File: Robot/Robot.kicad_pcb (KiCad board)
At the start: 2 copper layers, 130 x 156 mm, 172 parts, among them J1 Servo1, J10 Lidar, J11 Console, J12 M1, J13 M2, J14 M3, J15 M4, J16 Battery, J17 DE9_Receptacle, J18 Balance, J2 Servo2, J3 Servo3, J4 Servo4, J5 Servo5, J6 Servo6, J7 Servo7, J8 Beacon, J9 DLED, Q1 DMP3036SSD, Q2 Si2003, SW1 User, SW2 Pwr, U1 ADC128D818, U10 SY8366HQQC, U11 SY8366HQQC, U12 SY8366HQQC, U13 INA180A2, U14 INA180A2, U15 INA180A2, U16 INA180A2, U2 MaixCAM2, U3 DRV8845RHHR, U4 ICE40UP5K-SG48ITR, U5 74HCT245, U6 MCP4728, U7 NC7SZ175, U8 TLV70212DBVR, U9 TMI6050-33

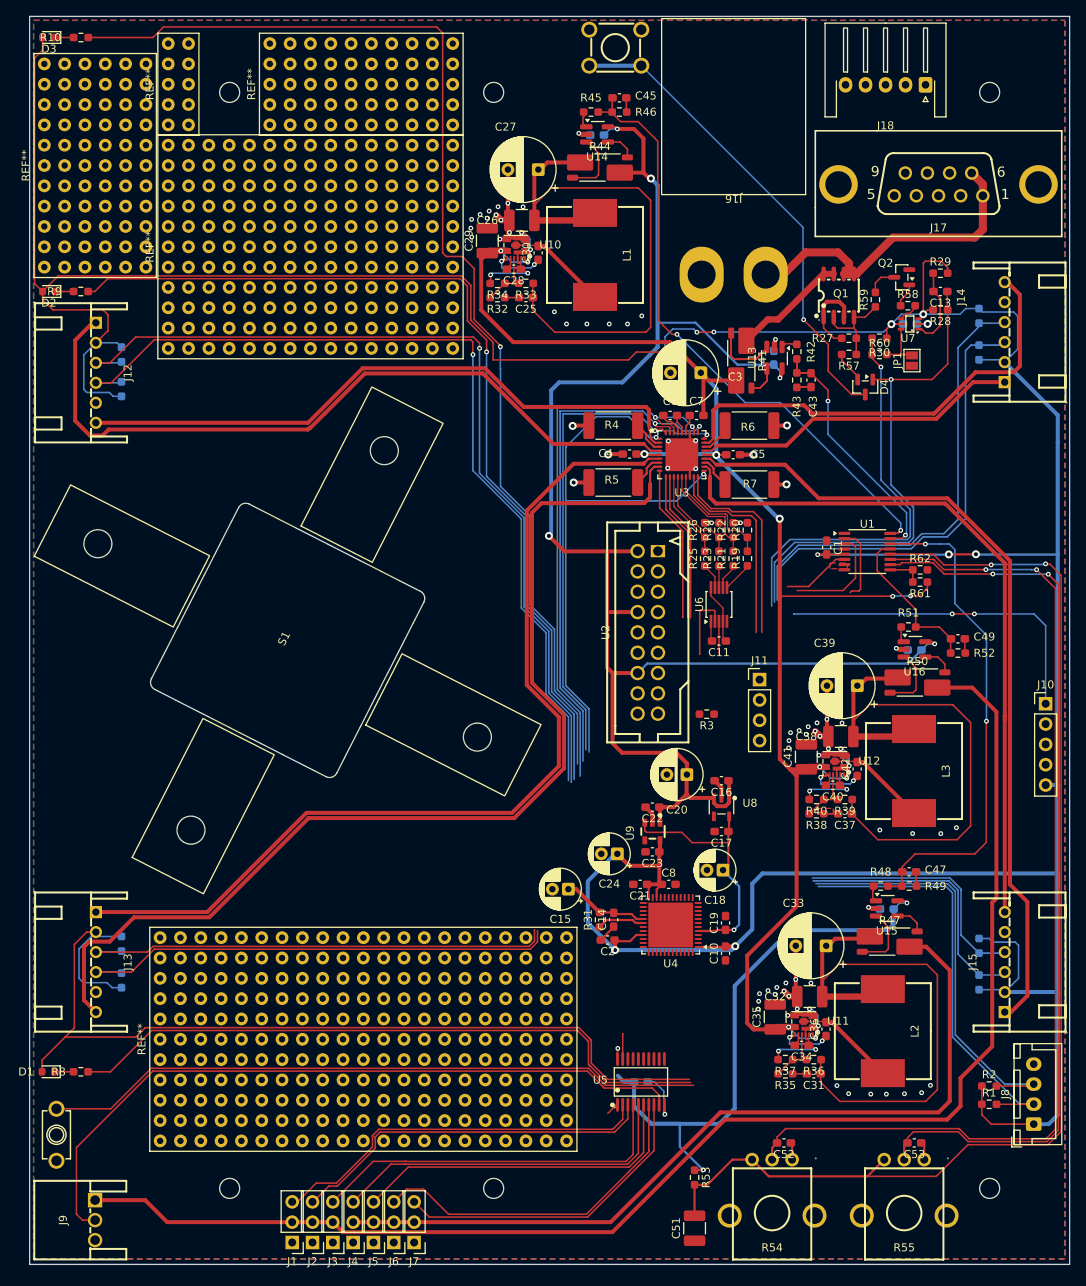
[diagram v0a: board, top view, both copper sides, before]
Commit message: Updated PCB for Robot (routing close to finish)
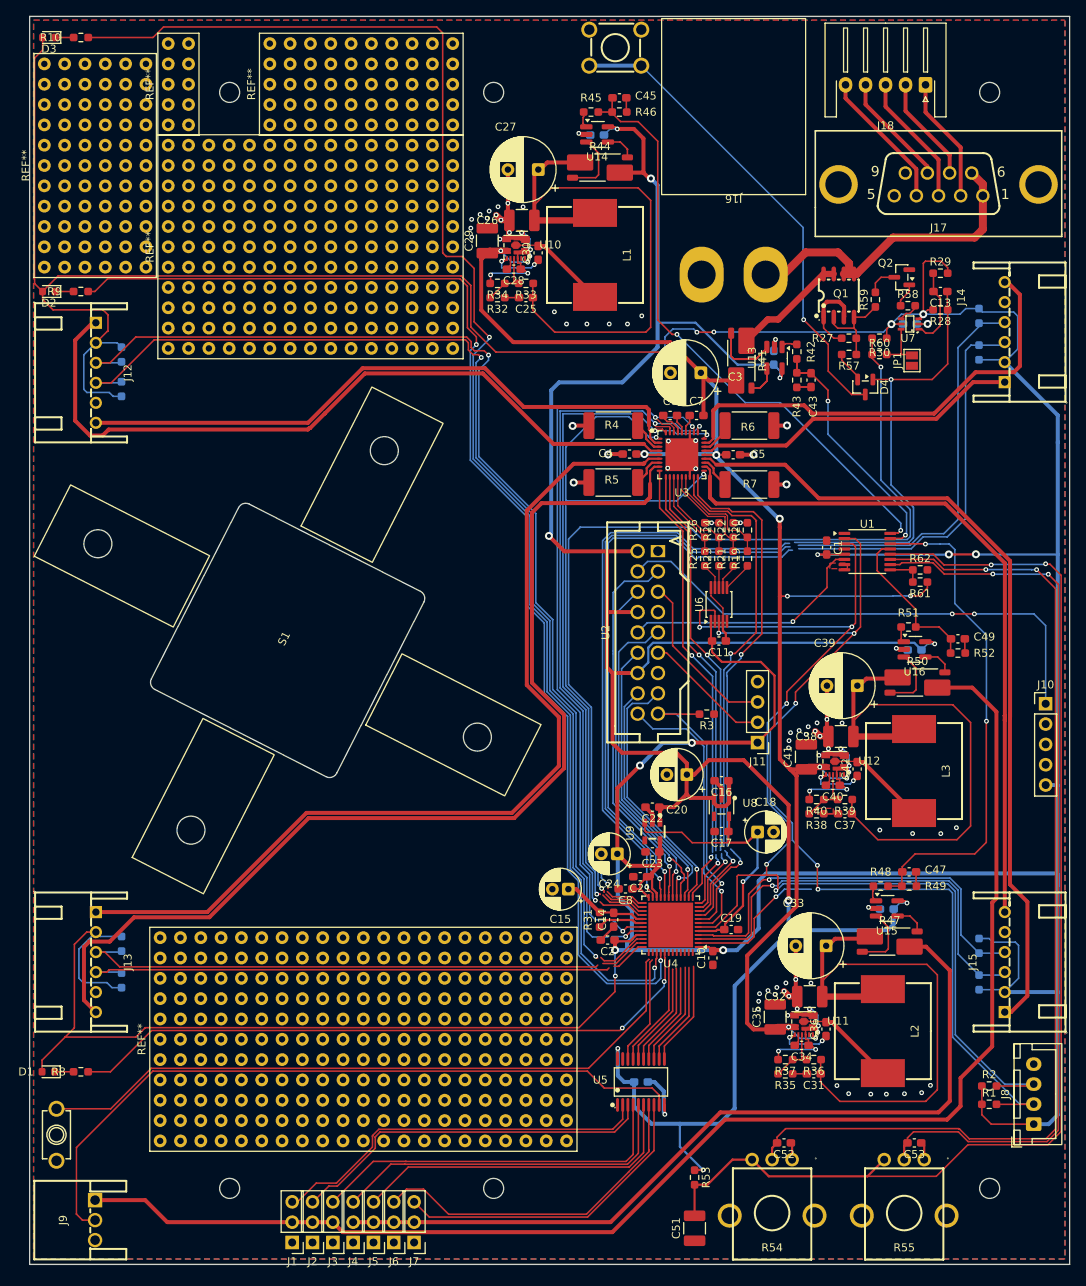
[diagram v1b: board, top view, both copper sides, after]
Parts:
- moved J11 7.88 mm to (126.0, 112.8), turned to 180 degrees
- moved C18 6.43 mm to (126.0, 124.0), turned to 0 degrees
- moved C8 5.43 mm to (109.5, 131.1), turned to 180 degrees
- moved C10 1.69 mm to (120.4, 139.7)
- moved C19 1.08 mm to (122.7, 136.1), turned to 0 degrees
- moved C21 0.95 mm to (111.3, 129.5)
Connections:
- R10 pad 2: Net-(U4A-RGB2) -> Net-(U4A-RGB0)
- R8 pad 2: Net-(U4A-RGB0) -> Net-(U4A-RGB2)
- U2 pad 3: /FPGA/CTRL_SYN -> /FPGA/CTRL_INT
- U2 pad 9: /FPGA/CTRL_INT -> /FPGA/CTRL_SYN
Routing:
- net Net-(U4A-RGB0): track 81.8 -> 184.3 mm, vias 0 -> 2
- net Net-(U3-PHASE1): track 25.6 -> 126.3 mm, vias 0 -> 2
- net Net-(U4B-IOB_23b): track 0.00 -> 85.0 mm, vias 0 -> 1
- net /FPGA/PWR_OFF: track 51.2 -> 126.9 mm, vias 1 -> 3
- net Net-(U4B-IOB_25b_G3): track 82.6 -> 157.4 mm, vias 0 -> 1
- net /FPGA/SCL: track 74.9 -> 148.8 mm, vias 0 -> 5
- net /FPGA/SDA: track 66.9 -> 136.7 mm, vias 0 -> 6
- net Net-(U4A-RGB2): track 144.7 -> 80.8 mm, vias 1 -> 2
- net /FPGA/CTRL_INT: track 0.00 -> 47.8 mm, vias 0 -> 1
- net /FPGA/DL_CS: track 0.00 -> 43.3 mm, vias 0 -> 1
- net /FPGA/CTRL_SYN: track 0.00 -> 39.8 mm, vias 0 -> 1
- net +3V3: track 620.5 -> 658.7 mm, vias 10 -> 13
- net Net-(U4A-RGB1): track 115.6 -> 153.8 mm, vias 1 -> 2
- net /FPGA/DL_CRESET: track 0.00 -> 37.5 mm, vias 0 -> 1
- net Net-(U3-PHASE4): track 19.6 -> 57.0 mm, vias 0 -> 1
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
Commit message: Updated PCB for Robot (routing finished, postprocessing in progress)
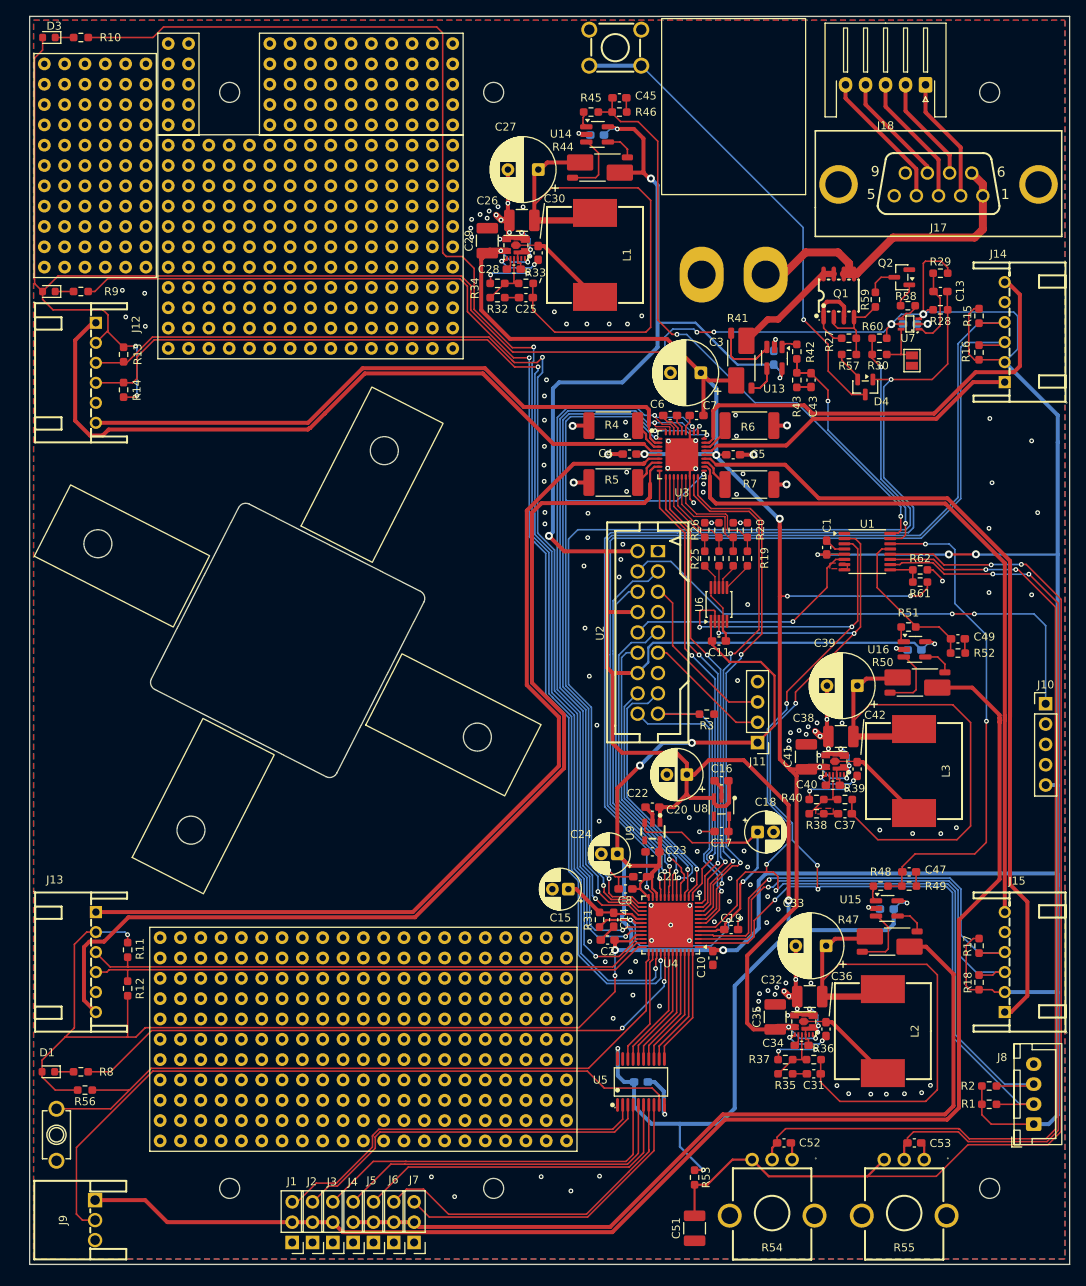
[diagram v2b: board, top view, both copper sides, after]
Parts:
- added R56: 1K, Resistor_SMD:R_0603_1608Metric_Pad0.98x0.95mm_HandSolder, F.Cu at (41.9, 156.2)
- J12, J13, J14, J15: footprint easyeda2kicad:CONN-TH_S6B-XH-A-1-LF-SN -> locals:CONN-TH_S6B-XH-A-1-LF-SN
- R11, R12, R13, R14, R15, R16, R17, R18: moved to F.Cu
- R54, R55: footprint easyeda2kicad:RES-TH_RK09K1130A6S -> locals:RES-TH_RK09K1130A6S
- moved R12 1.27 mm to (47.2, 143.5)
- moved R11 1.08 mm to (47.2, 138.7)
- moved R14 0.28 mm to (46.7, 68.7)
- moved R13 0.26 mm to (46.7, 64.3)
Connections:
- net Net-(J15A-C1) renamed /FPGA/FPGACore/P4
- net Net-(J15A-C2) renamed /FPGA/FPGACore/P3
- net Net-(U4A-IOT_49a) renamed /FPGA/FPGACore/P43
- J12 pad 3: Net-(J12A-C2) -> /FPGA/FPGACore/P32
- J12 pad 4: Net-(J12A-C1) -> /FPGA/FPGACore/P34
- J13 pad 3: Net-(J13A-C2) -> /FPGA/FPGACore/P35
- J13 pad 4: Net-(J13A-C1) -> /FPGA/FPGACore/P36
- J14 pad 3: Net-(J14A-C2) -> /FPGA/FPGACore/P20
- J14 pad 4: Net-(J14A-C1) -> /FPGA/FPGACore/P21
- R11 pad 1: Net-(J13A-C2) -> /FPGA/FPGACore/P35
- R12 pad 1: Net-(J13A-C1) -> /FPGA/FPGACore/P36
- R13 pad 1: Net-(J12A-C2) -> /FPGA/FPGACore/P32
- R14 pad 1: Net-(J12A-C1) -> /FPGA/FPGACore/P34
- R15 pad 1: Net-(J14A-C1) -> /FPGA/FPGACore/P21
- R16 pad 1: Net-(J14A-C2) -> /FPGA/FPGACore/P20
- SW1 pad 2: Net-(U4B-IOB_25b_G3) -> /FPGA/FPGACore/P37
- U3 pad 1: Net-(U3-I04) -> /FPGA/FPGACore/P26
- U3 pad 10: Net-(U3-PHASE3) -> /FPGA/FPGACore/P12
- U3 pad 11: Net-(U3-~{SLEEP}) -> /FPGA/FPGACore/P11
- U3 pad 17: Net-(U3-PHASE2) -> /FPGA/FPGACore/P10
- U3 pad 18: Net-(U3-PHASE1) -> /FPGA/FPGACore/P9
- U3 pad 19: Net-(U3-I04) -> /FPGA/FPGACore/P26
- U3 pad 27: Net-(U3-I03) -> /FPGA/FPGACore/P27
- U3 pad 28: Net-(U3-I02) -> /FPGA/FPGACore/P28
- U3 pad 29: Net-(U3-I01) -> /FPGA/FPGACore/P31
- U3 pad 34: Net-(U3-I01) -> /FPGA/FPGACore/P31
- U3 pad 35: Net-(U3-I02) -> /FPGA/FPGACore/P28
- U3 pad 36: Net-(U3-I03) -> /FPGA/FPGACore/P27
- U3 pad 9: Net-(U3-PHASE4) -> /FPGA/FPGACore/P13
- U4 pad 10: /FPGA/PWR_OFF -> /FPGA/FPGACore/P10
- U4 pad 11: Net-(U4B-IOB_20a) -> /FPGA/FPGACore/P11
- U4 pad 12: Net-(U4B-IOB_22a) -> /FPGA/FPGACore/P12
- U4 pad 13: /FPGA/PwrBtnInput -> /FPGA/FPGACore/P13
- U4 pad 2: Net-(J14A-C2) -> /FPGA/SDA
- U4 pad 20: Net-(U4B-IOB_25b_G3) -> /FPGA/FPGACore/P20
- U4 pad 21: Net-(U4B-IOB_23b) -> /FPGA/FPGACore/P21
- U4 pad 23: Net-(U3-PHASE1) -> /FPGA/PwrBtnInput
- U4 pad 25: Net-(U3-I01) -> /FPGA/PWR_OFF
- U4 pad 26: Net-(U3-PHASE2) -> /FPGA/FPGACore/P26
- U4 pad 27: Net-(U3-I02) -> /FPGA/FPGACore/P27
- U4 pad 28: Net-(U3-I03) -> /FPGA/FPGACore/P28
- U4 pad 31: Net-(U3-PHASE3) -> /FPGA/FPGACore/P31
- U4 pad 32: Net-(U3-I04) -> /FPGA/FPGACore/P32
- U4 pad 34: Net-(U3-PHASE4) -> /FPGA/FPGACore/P34
- U4 pad 35: Net-(U4A-IOT_46b_G0) -> /FPGA/FPGACore/P35
- U4 pad 36: Net-(U4A-IOT_48b) -> /FPGA/FPGACore/P36
- U4 pad 37: Net-(U3-~{SLEEP}) -> /FPGA/FPGACore/P37
- U4 pad 38: Net-(U4A-IOT_50b) -> /FPGA/FPGACore/P38
- U4 pad 42: Net-(U4A-IOT_51a) -> /FPGA/FPGACore/P42
- U4 pad 44: Net-(J13A-C1) -> /FPGA/FPGACore/P44
- U4 pad 45: Net-(J14A-C1) -> /FPGA/FPGACore/P45
- U4 pad 46: Net-(J12A-C1) -> /FPGA/FPGACore/P46
- U4 pad 47: Net-(J12A-C2) -> /FPGA/FPGACore/P47
- U4 pad 48: Net-(J13A-C2) -> /FPGA/FPGACore/P48
- U4 pad 9: /FPGA/SDA -> /FPGA/FPGACore/P9
- U5 pad 11: Net-(U4B-IOB_23b) -> /FPGA/FPGACore/P48
- U5 pad 12: Net-(U4B-IOB_22a) -> /FPGA/FPGACore/P47
- U5 pad 13: Net-(U4B-IOB_20a) -> /FPGA/FPGACore/P46
- U5 pad 14: Net-(U4A-IOT_51a) -> /FPGA/FPGACore/P45
- U5 pad 15: Net-(U4A-IOT_50b) -> /FPGA/FPGACore/P44
- U5 pad 17: Net-(U4A-IOT_48b) -> /FPGA/FPGACore/P42
- U5 pad 18: Net-(U4A-IOT_46b_G0) -> /FPGA/FPGACore/P38
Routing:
- net Net-(U4B-IOB_25b_G3): track 157.4 -> 0.00 mm, vias 1 -> 0
- net /FPGA/FPGACore/P34: track 0.00 -> 144.3 mm, vias 0 -> 2
- net /FPGA/FPGACore/P32: track 0.00 -> 140.5 mm, vias 0 -> 2
- net Net-(J12A-C1): track 136.8 -> 0.00 mm, vias 2 -> 0
- net Net-(J12A-C2): track 136.1 -> 0.00 mm, vias 1 -> 0
- net Net-(U3-PHASE1): track 126.3 -> 0.00 mm, vias 2 -> 0
- net /FPGA/FPGACore/P21: track 0.00 -> 122.9 mm, vias 0 -> 1
- net /FPGA/FPGACore/P20: track 0.00 -> 121.5 mm, vias 0 -> 1
- net /FPGA/FPGACore/P26: track 0.00 -> 99.1 mm, vias 0 -> 3
- net Net-(U3-I04): track 95.8 -> 0.00 mm, vias 4 -> 0
- net /FPGA/FPGACore/P31: track 0.00 -> 95.1 mm, vias 0 -> 3
- net Net-(U3-I01): track 94.9 -> 0.00 mm, vias 2 -> 0
- net Net-(U3-I02): track 91.6 -> 0.00 mm, vias 3 -> 0
- net /FPGA/FPGACore/P28: track 0.00 -> 91.6 mm, vias 0 -> 3
- net /FPGA/FPGACore/P37: track 0.00 -> 90.8 mm
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
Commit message: Finished PCB for Robot
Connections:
- REF** pad 105: (no net) -> +12V
- REF** pad 120: (no net) -> +12V
- REF** pad 150: (no net) -> +5V
- REF** pad 165: (no net) -> +5V
- REF** pad 43: (no net) -> GND
- REF** pad 44: (no net) -> GND
- REF** pad 45: (no net) -> GND
- REF** pad 73: (no net) -> +3V3
- REF** pad 74: (no net) -> +3V3
- REF** pad 75: (no net) -> +3V3
- REF** pad 90: (no net) -> +12V
- REF** pad 145: (no net) -> +3V3
- REF** pad 146: (no net) -> +3V3
- REF** pad 147: (no net) -> +3V3
- REF** pad 166: (no net) -> GND
- REF** pad 167: (no net) -> GND
- REF** pad 168: (no net) -> GND
- REF** pad 229: (no net) -> GND
- REF** pad 230: (no net) -> GND
- REF** pad 231: (no net) -> GND
- REF** pad 40: (no net) -> +5V
- REF** pad 41: (no net) -> +5V
- REF** pad 42: (no net) -> +5V
- REF** pad 82: (no net) -> +12V
- REF** pad 83: (no net) -> +12V
- REF** pad 84: (no net) -> +12V
- REF** pad 10: (no net) -> +5V
- REF** pad 30: (no net) -> GND
- REF** pad 40: (no net) -> GND
- REF** pad 50: (no net) -> GND
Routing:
- net +5V: track 316.7 -> 364.3 mm
- net +12V: track 201.3 -> 243.4 mm
- net Net-(J18-Pin_5): track 17.5 -> 25.7 mm
- net /FPGA/DLED: track 90.3 -> 88.3 mm
- net +3V3: track 660.8 -> 661.6 mm
- net Net-(U4A-RGB0): track 184.5 -> 183.8 mm
- net GND: vias 165 -> 374
